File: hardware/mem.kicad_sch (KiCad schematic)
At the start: 4 parts, among them U6 74HC00

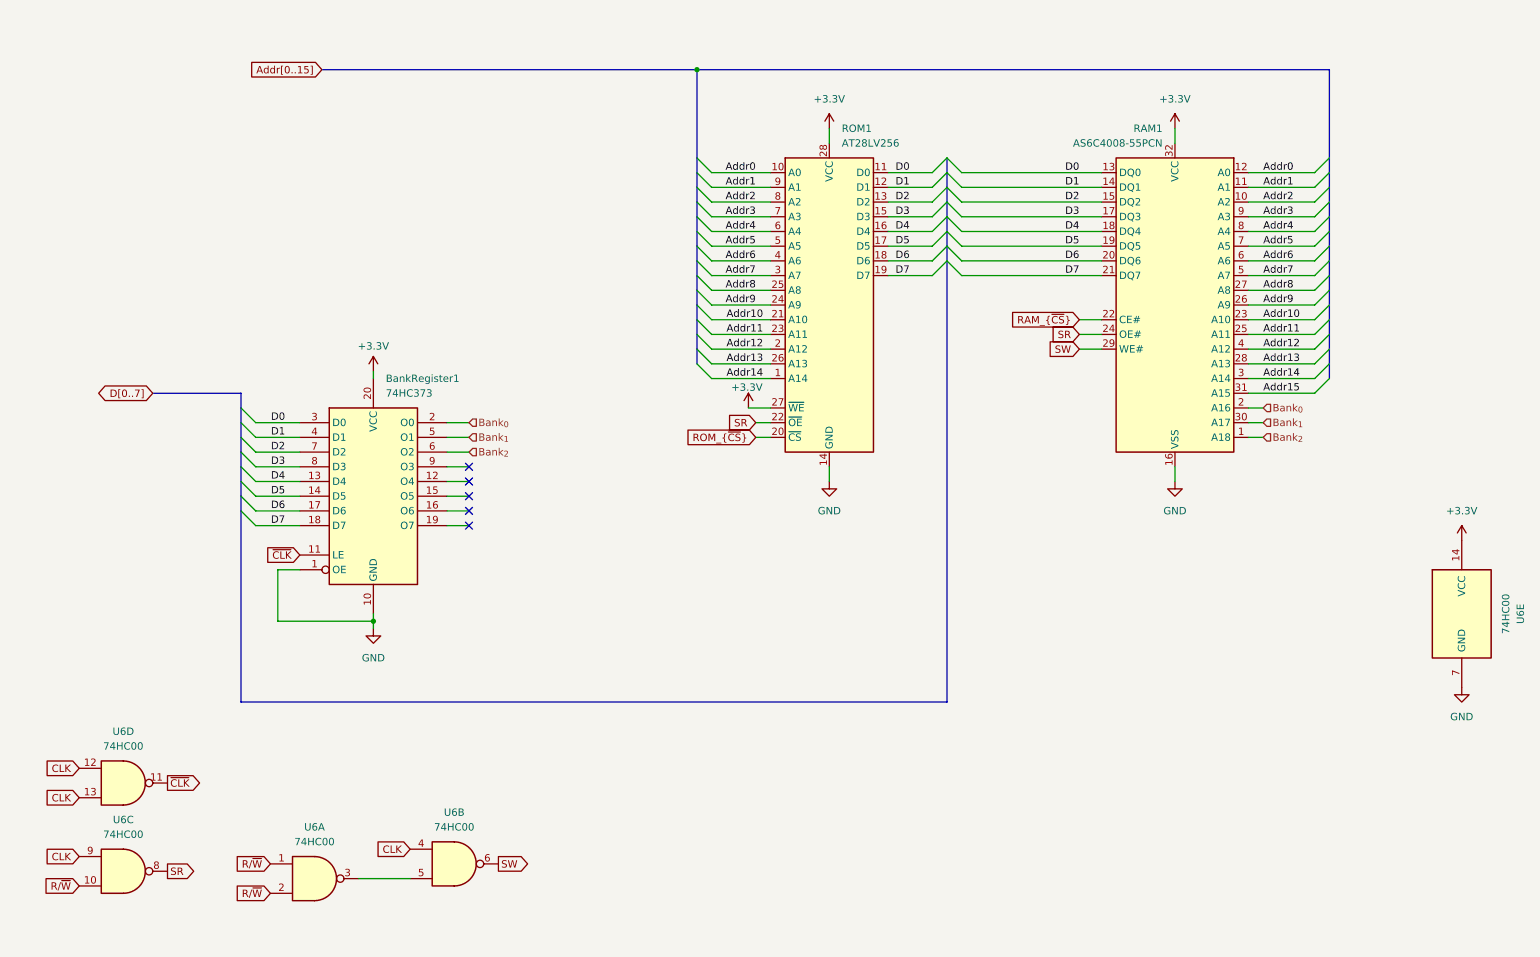
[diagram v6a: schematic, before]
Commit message: Removed old VPU
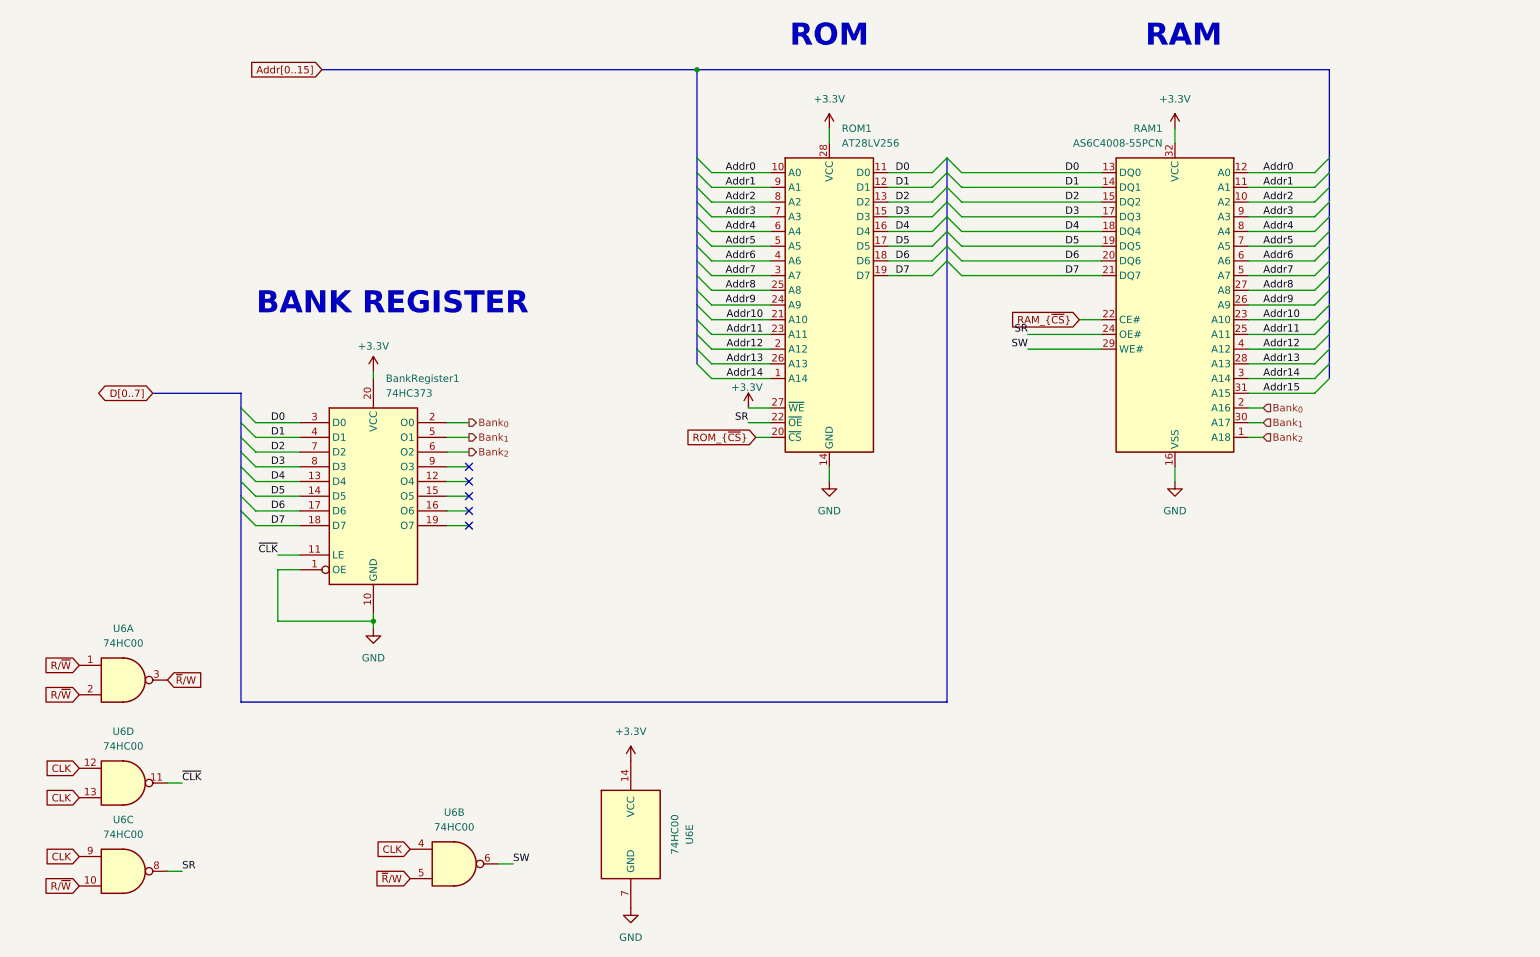
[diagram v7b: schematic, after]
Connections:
- net ~{R}/W: now reaches U6.3, U6.5
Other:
- note added: "BANK REGISTER"
- note added: "RAM"
- note added: "ROM"
- moved on the sheet: U6E
